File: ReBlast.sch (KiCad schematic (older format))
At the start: 23 parts, among them J1 MOS_8580_Socket, U1 74HC20, U2 74HC139, U3 ZN428E-8, U4 TLC272, U5 MOS_8580, U6 ADC0804

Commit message: Fix DRC
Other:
- note added: "Note we must NOT enable SID for\nthe addresses we "steal"!"
- note removed: "Note we must NOT enable SID for\nthe addresses we "steal"!\n(Thanks TLC)"
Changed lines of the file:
@@
 ADDRESS DECODING
 Text Notes 4030 7310 0    50   ~ 0
-Note we must NOT enable SID for\nthe addresses we "steal"!\n(Thanks TLC)
+Note we must NOT enable SID for\nthe addresses we "steal"!
 Text Label 12565 4945 2    50   ~ 0
 dac_output

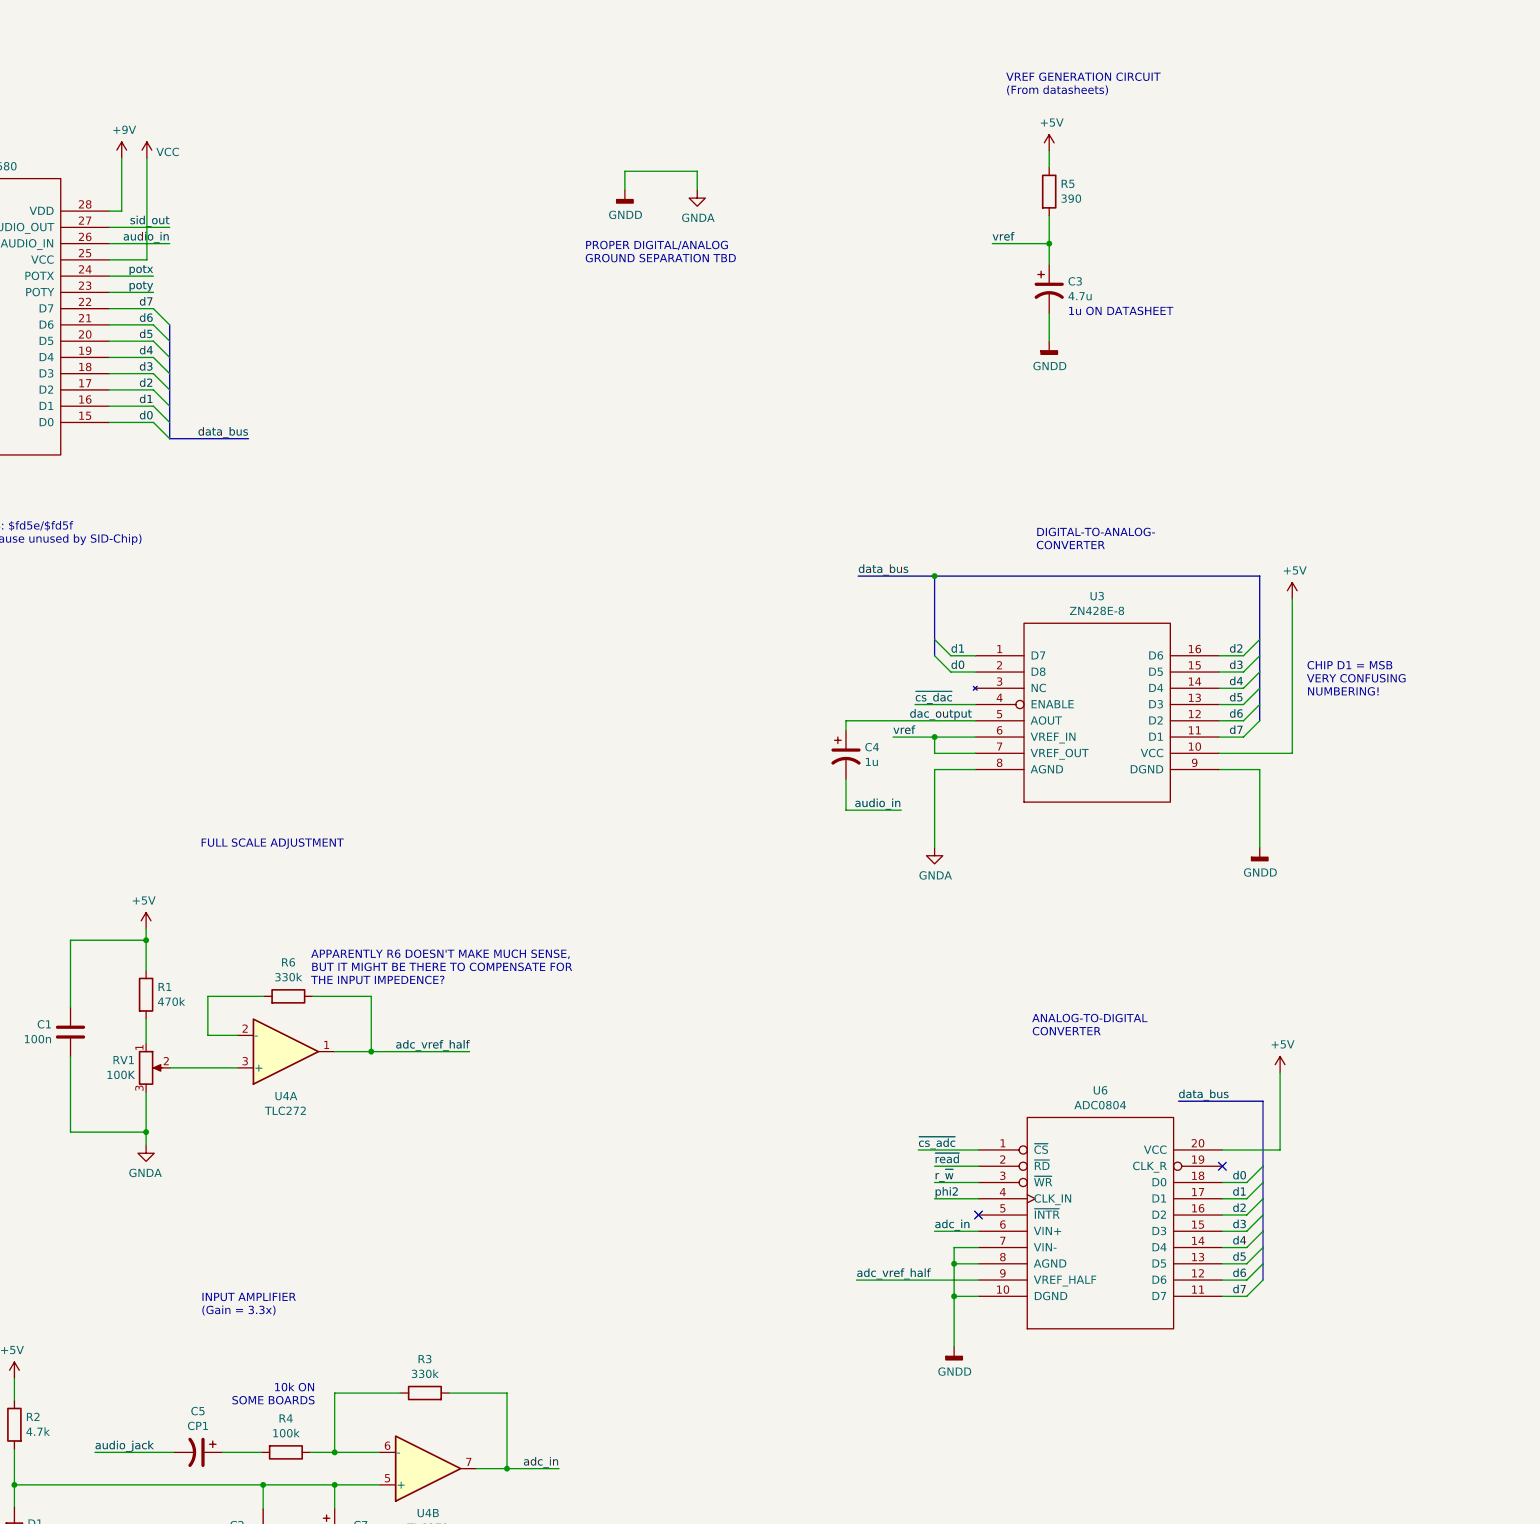
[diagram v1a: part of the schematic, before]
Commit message: Add some notes, fix ERC, adjust some tracks
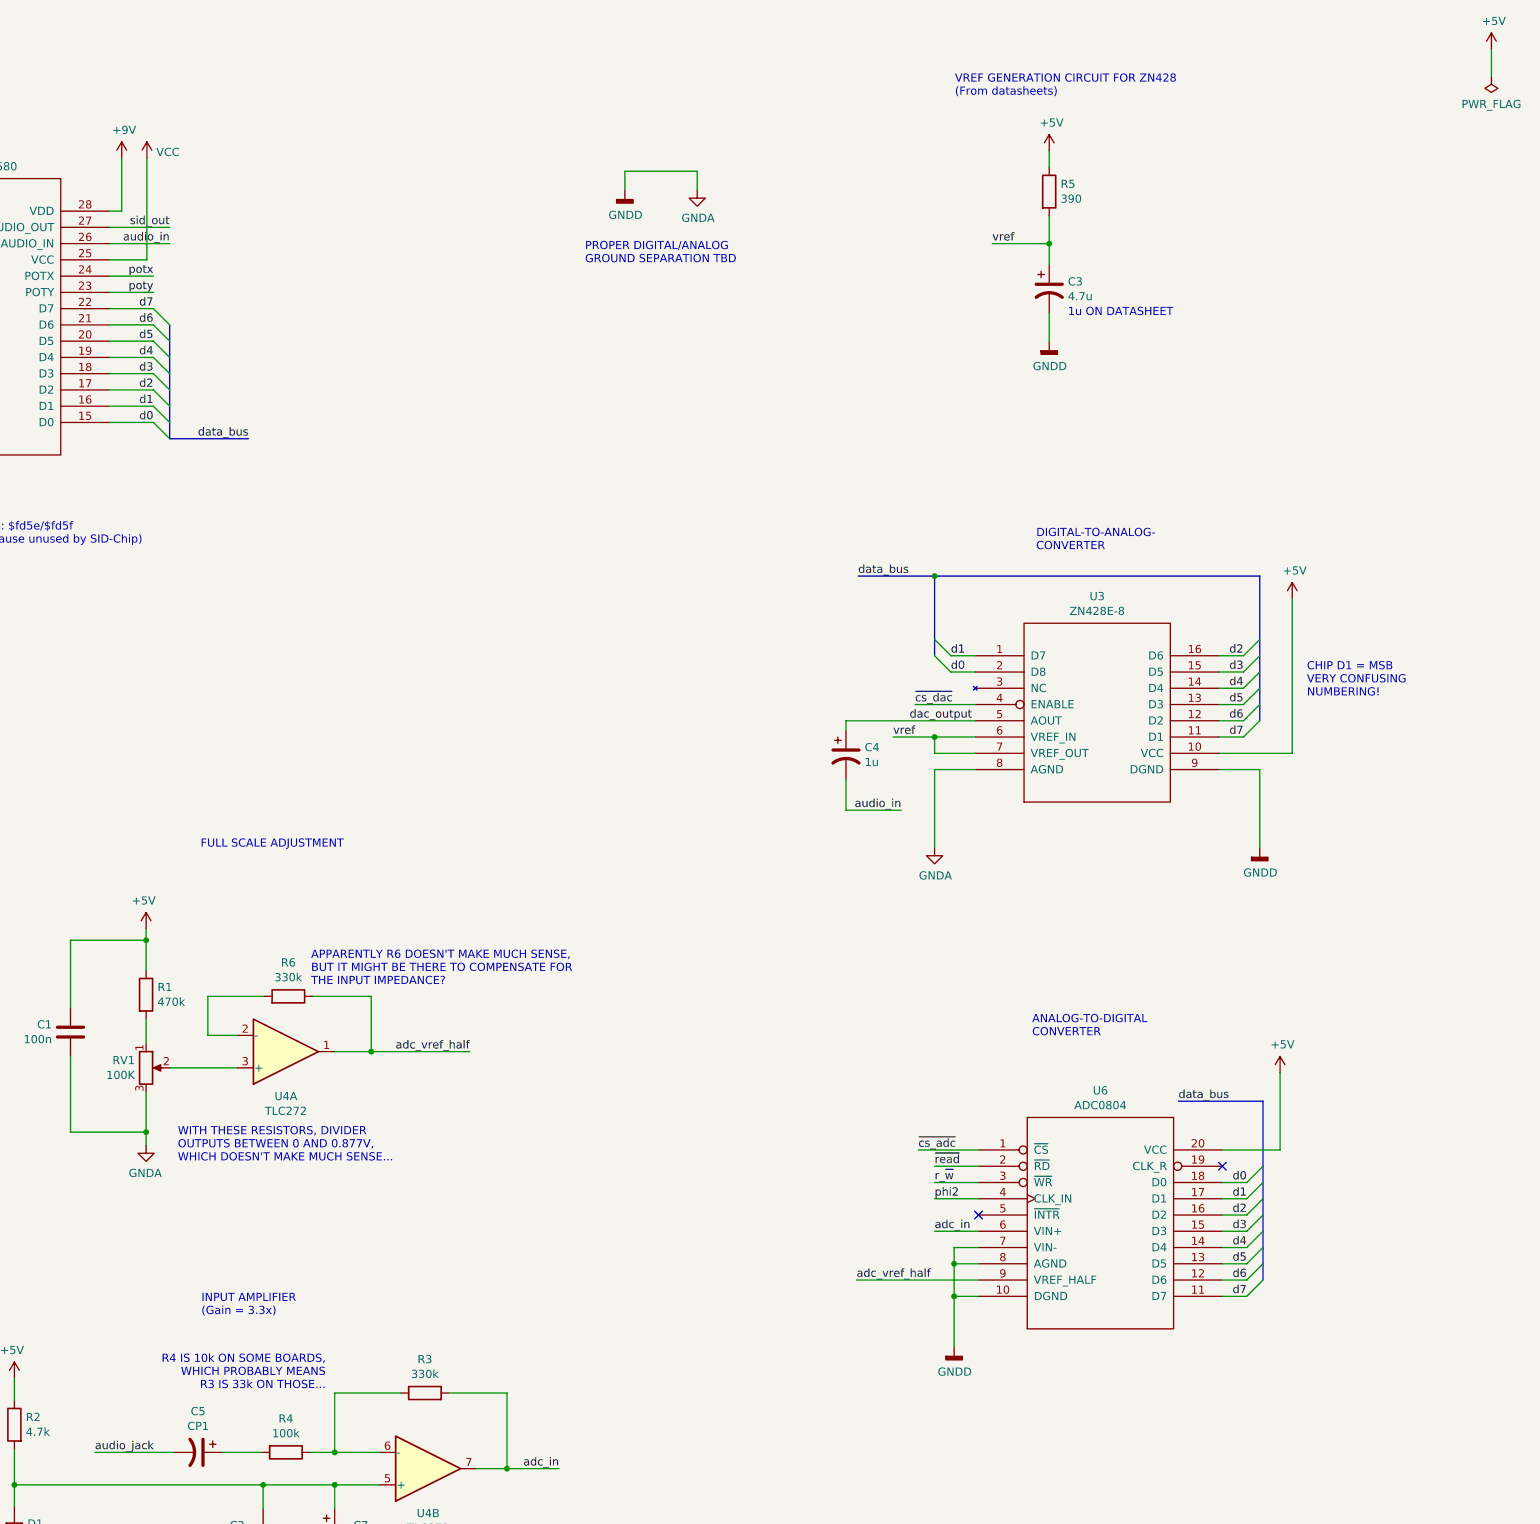
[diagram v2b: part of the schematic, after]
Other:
- note added: "APPARENTLY R6 DOESN'T MAKE MUCH SENSE,\nBUT IT MIGHT BE THERE TO COMPENSATE FOR\nTHE INPUT IMPEDANCE?"
- note added: "R4 IS 10k ON SOME BOARDS,\nWHICH PROBABLY MEANS\nR3 IS 33k ON THOSE..."
- note added: "VREF GENERATION CIRCUIT FOR ZN428\n(From datasheets)"
- note added: "WITH THESE RESISTORS, DIVIDER\nOUTPUTS BETWEEN 0 AND 0.877V,\nWHICH DOESN'T MAKE MUCH SENSE..."
- note removed: "10k ON\nSOME BOARDS"
- note removed: "APPARENTLY R6 DOESN'T MAKE MUCH SENSE,\nBUT IT MIGHT BE THERE TO COMPENSATE FOR\nTHE INPUT IMPEDENCE?"
- note removed: "VREF GENERATION CIRCUIT\n(From datasheets)"
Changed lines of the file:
@@
 Sheet 1 1
 Title "ReBlast"
-Date "2024-02-29"
+Date "2024-03-03"
 Rev "1git"
 Comp "SukkoPera"
@@
 Wire Wire Line
 	13040 2010 13040 2140
-Text Notes 12775 1105 0    50   ~ 0
-VREF GENERATION CIRCUIT\n(From datasheets)
+Text Notes 12460 1110 0    50   ~ 0
+VREF GENERATION CIRCUIT FOR ZN428\n(From datasheets)
 Wire Wire Line
 	12335 5245 12335 5725
@@
 	9705 9545 10025 9545
 Connection ~ 9705 9545
-Text Notes 8525 9165 2    50   ~ 0
-10k ON\nSOME BOARDS
+Text Notes 8590 9065 2    50   ~ 0
+R4 IS 10k ON SOME BOARDS,\nWHICH PROBABLY MEANS\nR3 IS 33k ON THOSE...
 $Comp
 L Device:R R6
@@
 adc_vref_half
 Text Notes 8500 6580 0    50   ~ 0
-APPARENTLY R6 DOESN'T MAKE MUCH SENSE,\nBUT IT MIGHT BE THERE TO COMPENSATE FOR\nTHE INPUT IMPEDENCE?
+APPARENTLY R6 DOESN'T MAKE MUCH SENSE,\nBUT IT MIGHT BE THERE TO COMPENSATE FOR\nTHE INPUT IMPEDANCE?
 Wire Wire Line
 	3100 8000 2610 8000
@@
 Text Notes 7820 5735 0    50   ~ 0
 FULL SCALE ADJUSTMENT
+Text Notes 7680 7665 0    50   ~ 0
+WITH THESE RESISTORS, DIVIDER\nOUTPUTS BETWEEN 0 AND 0.877V,\nWHICH DOESN'T MAKE MUCH SENSE...
+$Comp
+L power:+5V #PWR0131
+U 1 1 65EAE98B
+P 15760 815
+F 0 "#PWR0131" H 15760 665 50  0001 C CNN
+F 1 "+5V" H 15775 988 50  0000 C CNN
+F 2 "" H 15760 815 50  0001 C CNN
+F 3 "" H 15760 815 50  0001 C CNN
+	1    15760 815
+	1    0    0    -1
+$EndComp
+$Comp
+L power:PWR_FLAG #FLG0102
+U 1 1 65EBC254
+P 15760 980
+F 0 "#FLG0102" H 15760 1055 50  0001 C CNN
+F 1 "PWR_FLAG" H 15760 1153 50  0000 C CNN
+F 2 "" H 15760 980 50  0001 C CNN
+F 3 "~" H 15760 980 50  0001 C CNN
+	1    15760 980
+	-1   0    0    1
+$EndComp
+Wire Wire Line
+	15760 980  15760 815
 Wire Bus Line
 	12335 4055 12335 4545

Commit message: AT LAAAAAAAAAST! Though I must admit that R6 is really misleading...
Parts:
- C5: value CP1 -> 1u
- D1: value 2.5V ZENER -> 1n4148
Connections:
- net adc_vref_half: now also C2.1, D1.2 (A), R2.2; no longer R6.1, U4.1
- net opamp_bias: now reaches RV1.2, U4.3 (+)
- net opamp_bias: now also C7.1, U4.5 (+)
- new net: R6.1, U4.1
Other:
- note added: "ABOUT 0.7V\n(DIODE DROP)"
- note added: "ADC INPUT AMPLIFIER\n(Gain = 3.3x)"
- note added: "ADC VREF GENERATION"
- note added: "OFFSET CAN BE SET BETWEEN 0\nAND 0.877V, WHICH IS COHERENT\nWITH THE 0.7V VREF"
- note added: "PROBABLY OTHER\n"COMMON" DIODES\nWILL DO"
- note added: "UNUSED OPAMP\n(WEIRD CONFIGURATION...)"
- note removed: "APPARENTLY R6 DOESN'T MAKE MUCH SENSE,\nBUT IT MIGHT BE THERE TO COMPENSATE FOR\nTHE INPUT IMPEDANCE?"
- note removed: "FULL SCALE ADJUSTMENT"
- note removed: "INPUT AMPLIFIER\n(Gain = 3.3x)"
- note removed: "TOO BAD THIS ZENER\nDIODE IS BACKWARDS..."
- note removed: "WITH THESE RESISTORS, DIVIDER\nOUTPUTS BETWEEN 0 AND 0.877V,\nWHICH DOESN'T MAKE MUCH SENSE..."
- moved on the sheet: C1, C2, C5, C7, D1, R1, R2, R3, R4, R6, RV1, U4A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

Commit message: Almost there...
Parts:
- removed R6: 330k, Resistor_THT:R_Axial_DIN0207_L6.3mm_D2.5mm_P2.54mm_Vertical, symbol Device:R
- added C10, C8, C9: 100n, Capacitor_THT:C_Disc_D7.0mm_W2.5mm_P5.00mm, symbol Device:C
- C1, C2: footprint Capacitor_THT:C_Disc_D5.0mm_W2.5mm_P2.50mm -> Capacitor_THT:C_Disc_D7.0mm_W2.5mm_P5.00mm
- D1: footprint Diode_THT:D_DO-35_SOD27_P7.62mm_Horizontal -> Diode_THT:D_DO-35_SOD27_P2.54mm_Vertical_KathodeUp
- L1: footprint Inductor_THT:L_Axial_L6.6mm_D2.7mm_P10.16mm_Horizontal_Vishay_IM-2 -> Inductor_THT:L_Radial_D6.0mm_P4.00mm
- R1, R2, R4, R5: footprint Resistor_THT:R_Axial_DIN0204_L3.6mm_D1.6mm_P7.62mm_Horizontal -> Resistor_THT:R_Axial_DIN0207_L6.3mm_D2.5mm_P2.54mm_Vertical
- RV1: footprint Potentiometer_THT:Potentiometer_ACP_CA14V-15_Vertical -> ReBlast:Pot_Bourns_3306P
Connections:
- net +5V: now also C10.1
- net GNDA: now also C10.2, C8.2, C9.2
- net VCC: now also C8.1, C9.1
- net adc_in: now also R3.1; no longer R3.2
- net at U4.1: now also U4.2 (-)
- net at R4.1, U4.6 (-): now also R3.2; no longer R3.1
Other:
- note added: "DECOUPLING"
- note added: "POWER"
- note removed: "TODO: Add 100nF caps for U1/U2"
- moved on the sheet: C1, C5, C6, C7, L1, R1, R3, R4, RV1, U4B

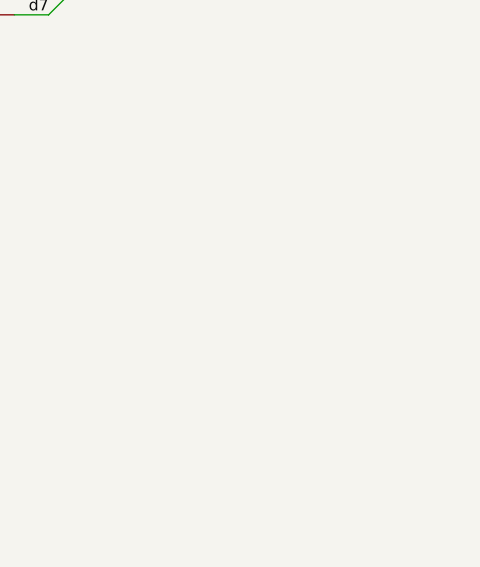
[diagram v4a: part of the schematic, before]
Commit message: Add logo, etc.
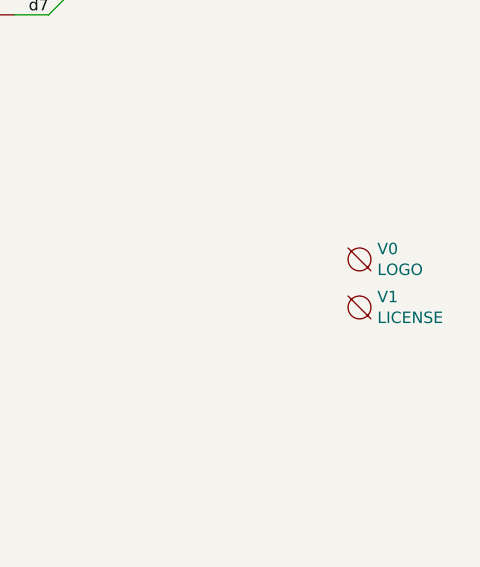
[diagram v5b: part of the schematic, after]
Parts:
- added V0: LOGO, ReBlast:logo, symbol void:Void
- added V1: LICENSE, ReBlast:cc_by_nc_sa_small, symbol void:Void
- U6: footprint Package_DIP:DIP-20_W7.62mm -> Package_DIP:DIP-20_W7.62mm_Socket
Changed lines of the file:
@@
 Sheet 1 1
 Title "ReBlast"
-Date "2024-03-23"
+Date "2024-04-06"
 Rev "1git"
 Comp "SukkoPera"
@@
 F 0 "U6" H 13355 8850 50  0000 C CNN
 F 1 "ADC0804" H 13355 8759 50  0000 C CNN
-F 2 "Package_DIP:DIP-20_W7.62mm" H 13355 8035 50  0001 C CNN
+F 2 "Package_DIP:DIP-20_W7.62mm_Socket" H 13355 8035 50  0001 C CNN
 F 3 "DOCUMENTATION" H 13355 8035 50  0001 C CNN
 	1    13355 8035
@@
 POWER
 $Comp
-L power:GNDA #PWR?
+L power:GNDA #PWR0133
 U 1 1 66162F1E
 P 4720 10785
-F 0 "#PWR?" H 4720 10535 50  0001 C CNN
+F 0 "#PWR0133" H 4720 10535 50  0001 C CNN
 F 1 "GNDA" H 4725 10612 50  0000 C CNN
 F 2 "" H 4720 10785 50  0001 C CNN
@@
 $EndComp
 $Comp
-L power:VCC #PWR?
+L power:VCC #PWR0134
 U 1 1 66163312
 P 3585 10260
-F 0 "#PWR?" H 3585 10110 50  0001 C CNN
+F 0 "#PWR0134" H 3585 10110 50  0001 C CNN
 F 1 "VCC" H 3600 10433 50  0000 C CNN
 F 2 "" H 3585 10260 50  0001 C CNN
@@
 $EndComp
 $Comp
-L power:VCC #PWR?
+L power:VCC #PWR0135
 U 1 1 66163970
 P 4145 10260
-F 0 "#PWR?" H 4145 10110 50  0001 C CNN
+F 0 "#PWR0135" H 4145 10110 50  0001 C CNN
 F 1 "VCC" H 4160 10433 50  0000 C CNN
 F 2 "" H 4145 10260 50  0001 C CNN
@@
 Wire Bus Line
 	14355 7285 14355 8385
+$Comp
+L void:Void V1
+U 1 1 6613F482
+P 15615 9765
+F 0 "V1" H 15693 9811 50  0000 L CNN
+F 1 "LICENSE" H 15693 9720 50  0000 L CNN
+F 2 "ReBlast:cc_by_nc_sa_small" H 15615 9765 50  0001 C CNN
+F 3 "" H 15615 9765 50  0001 C CNN
+	1    15615 9765
+	1    0    0    -1
+$EndComp
+$Comp
+L void:Void V0
+U 1 1 6613FDFD
+P 15615 9555
+F 0 "V0" H 15693 9601 50  0000 L CNN
+F 1 "LOGO" H 15693 9510 50  0000 L CNN
+F 2 "ReBlast:logo" H 15615 9555 50  0001 C CNN
+F 3 "" H 15615 9555 50  0001 C CNN
+	1    15615 9555
+	1    0    0    -1
+$EndComp
 $EndSCHEMATC
